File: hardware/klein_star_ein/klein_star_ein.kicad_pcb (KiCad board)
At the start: 6 copper layers, 100 x 90 mm, 138 parts, among them J1 USB_A, J10 AudioJack3_Ground_Switch, J11 AudioJack3_Ground_Switch, J12 AudioJack3_Ground_Switch, J2 DB15_Female_HighDensity_Mount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, J3 Bus_PCI_Express_x1, J4 1367073-1, J5 ARJM11C7-502-AB-ER2-T, J6 USB_C_Receptacle, J7 MEM2051-00-195-00-A, J8 AudioJack3_Ground_Switch, J9 AudioJack3_Ground_Switch, U1 ECP5UM25, U10 SN74ALVC245PWR, U11 KSZ9021RL, U12 TUSB2036, U13 TPS2041B, U2 MT41K512M16, U3 MT41K512M16, U4 FT2232HQ, U5 W25Q128JVS, U6 USB3300-EZK, U7 USB3300-EZK, U8 SN74ALVC245PWR, U9 SN74ALVC245PWR

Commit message: Added decups to KSZ9021
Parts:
- added C67: 22uF, Capacitor_SMD:C_0402_1005Metric, F.Cu at (167.6, 35.6)
- added C68: 22uF, Capacitor_SMD:C_0402_1005Metric, F.Cu at (153.9, 26.6)
- added C69: 22uF, Capacitor_SMD:C_0402_1005Metric, F.Cu at (130.7, 52.7)
- added C70: 22uF, Capacitor_SMD:C_0402_1005Metric, F.Cu at (131.2, 34.5)
- added C71: 22uF, Capacitor_SMD:C_0402_1005Metric, F.Cu at (189.0, 42.7)
- added C72: 22uF, Capacitor_SMD:C_0402_1005Metric, F.Cu at (171.2, 34.7)
- added C73: 22uF, Capacitor_SMD:C_0402_1005Metric, F.Cu at (147.5, 30.9)
- added C74: 22uF, Capacitor_SMD:C_0402_1005Metric, F.Cu at (130.7, 50.7)
- added C75: 22uF, Capacitor_SMD:C_0402_1005Metric, F.Cu at (124.1, 33.9)
- added C76: 22uF, Capacitor_SMD:C_0402_1005Metric, F.Cu at (193.6, 42.6)
- added C77: 0.1uF, Capacitor_SMD:C_0402_1005Metric, F.Cu at (134.9, 114.5)
- added C78: 0.1uF, Capacitor_SMD:C_0402_1005Metric, F.Cu at (140.6, 116.5)
- added C79: 0.1uF, Capacitor_SMD:C_0402_1005Metric, F.Cu at (134.9, 112.5)
- added C80: 0.1uF, Capacitor_SMD:C_0402_1005Metric, F.Cu at (143.5, 112.5)
- added C81: 0.1uF, Capacitor_SMD:C_0402_1005Metric, F.Cu at (137.7, 114.5)
- added C82: 0.1uF, Capacitor_SMD:C_0402_1005Metric, F.Cu at (134.9, 116.5)
- added C83: 0.1uF, Capacitor_SMD:C_0402_1005Metric, F.Cu at (140.6, 114.5)
- added C84: 0.1uF, Capacitor_SMD:C_0402_1005Metric, F.Cu at (137.7, 112.5)
- added C85: 0.1uF, Capacitor_SMD:C_0402_1005Metric, F.Cu at (143.5, 114.5)
- added C86: 0.1uF, Capacitor_SMD:C_0402_1005Metric, F.Cu at (137.7, 116.5)
- added C87: 0.1uF, Capacitor_SMD:C_0402_1005Metric, F.Cu at (143.5, 116.5)
- added C88: 0.1uF, Capacitor_SMD:C_0402_1005Metric, F.Cu at (134.9, 118.5)
- added C89: 0.1uF, Capacitor_SMD:C_0402_1005Metric, F.Cu at (137.7, 118.5)
- added C90: 0.1uF, Capacitor_SMD:C_0402_1005Metric, F.Cu at (132.0, 118.5)
- added C91: 0.1uF, Capacitor_SMD:C_0402_1005Metric, F.Cu at (140.6, 112.5)
- added C92: 0.1uF, Capacitor_SMD:C_0402_1005Metric, F.Cu at (132.0, 114.5)
- added C93: 0.1uF, Capacitor_SMD:C_0402_1005Metric, F.Cu at (132.0, 116.5)
- added C94: 0.1uF, Capacitor_SMD:C_0402_1005Metric, F.Cu at (140.6, 118.5)
- added C95: 0.1uF, Capacitor_SMD:C_0402_1005Metric, F.Cu at (132.0, 112.5)
- added L3: 1uH, Inductor_SMD:L_0603_1608Metric, F.Cu at (170.7, 32.0)
- added L4: 1uH, Inductor_SMD:L_0603_1608Metric, F.Cu at (146.9, 27.3)
- added L5: 1uH, Inductor_SMD:L_0603_1608Metric, F.Cu at (127.8, 47.2)
- added L6: 1uH, Inductor_SMD:L_0603_1608Metric, F.Cu at (131.3, 31.8)
- added L7: 1uH, Inductor_SMD:L_0603_1608Metric, F.Cu at (194.4, 40.7)
- added R1: R220, Resistor_SMD:R_0402_1005Metric_Pad0.72x0.64mm_HandSolder, F.Cu at (116.5, 99.3)
- added R11: 200k, Resistor_SMD:R_0402_1005Metric_Pad0.72x0.64mm_HandSolder, F.Cu at (130.6, 48.6)
- added R12: 200k, Resistor_SMD:R_0402_1005Metric_Pad0.72x0.64mm_HandSolder, F.Cu at (127.5, 49.8)
- added R14: 200k, Resistor_SMD:R_0402_1005Metric_Pad0.72x0.64mm_HandSolder, F.Cu at (124.2, 29.8)
- added R15: 200k, Resistor_SMD:R_0402_1005Metric_Pad0.72x0.64mm_HandSolder, F.Cu at (127.5, 33.8)
- added R16: 200k, Resistor_SMD:R_0402_1005Metric_Pad0.72x0.64mm_HandSolder, F.Cu at (191.4, 40.6)
- added R17: 160k, Resistor_SMD:R_0402_1005Metric_Pad0.72x0.64mm_HandSolder, F.Cu at (194.8, 42.7)
- added R3: R220, Resistor_SMD:R_0402_1005Metric_Pad0.72x0.64mm_HandSolder, F.Cu at (116.2, 114.4)
- added R4: 200k, Resistor_SMD:R_0402_1005Metric_Pad0.72x0.64mm_HandSolder, F.Cu at (174.5, 31.6)
- added R6: 63.2k, Resistor_SMD:R_0402_1005Metric_Pad0.72x0.64mm_HandSolder, F.Cu at (174.1, 34.9)
- added R7: 200k, Resistor_SMD:R_0402_1005Metric_Pad0.72x0.64mm_HandSolder, F.Cu at (154.2, 28.7)
- added R8: 44.2k, Resistor_SMD:R_0402_1005Metric_Pad0.72x0.64mm_HandSolder, F.Cu at (151.5, 29.2)
- added TP3: TestPoint, TestPoint:TestPoint_Pad_1.0x1.0mm, F.Cu at (177.6, 30.9)
- added TP4: TestPoint, TestPoint:TestPoint_Pad_1.0x1.0mm, F.Cu at (150.1, 23.6)
- added TP5: TestPoint, TestPoint:TestPoint_Pad_1.0x1.0mm, F.Cu at (127.6, 52.2)
- added TP6: TestPoint, TestPoint:TestPoint_Pad_1.0x1.0mm, F.Cu at (130.8, 27.5)
- added TP7: TestPoint, TestPoint:TestPoint_Pad_1.0x1.0mm, F.Cu at (188.7, 40.5)
- added U14: AP61300Z6-7, Package_TO_SOT_SMD:SOT-563, F.Cu at (166.2, 32.9)
- added U15: AP61300Z6-7, Package_TO_SOT_SMD:SOT-563, F.Cu at (151.1, 27.4)
- added U16: AP61300Z6-7, Package_TO_SOT_SMD:SOT-563, F.Cu at (131.0, 46.3)
- added U17: AP61300Z6-7, Package_TO_SOT_SMD:SOT-563, F.Cu at (127.7, 30.5)
- added U18: AP61300Z6-7, Package_TO_SOT_SMD:SOT-563, F.Cu at (191.4, 42.8)
- moved C58 61.5 mm to (64.1, 116.8)
- moved U11 1.54 mm to (124.5, 106.5)
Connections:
- J5 pad L1: unconnected-(J5-PadL1) -> Net-(J5-PadL1)
- J5 pad L2: unconnected-(J5-PadL2) -> Net-(J5-PadL2)
- J5 pad L3: unconnected-(J5-PadL3) -> Net-(J5-PadL3)
- J5 pad L4: unconnected-(J5-PadL4) -> Net-(J5-PadL4)
- J5 pad S1: Net-(J5-PadS1) -> GND
- J5 pad S2: Net-(J5-PadS1) -> GND
- J6 pad A1: Net-(J6-PadA1) -> GND
- J6 pad A12: Net-(J6-PadA1) -> GND
- J6 pad A4: Net-(J6-PadA4) -> +5V
- J6 pad A9: Net-(J6-PadA4) -> +5V
- J6 pad B1: Net-(J6-PadA1) -> GND
- J6 pad B12: Net-(J6-PadA1) -> GND
- J6 pad B4: Net-(J6-PadA4) -> +5V
- J6 pad B9: Net-(J6-PadA4) -> +5V
- J6 pad S1: unconnected-(J6-PadS1) -> GND
- U11 pad 12: unconnected-(U11-Pad12) -> +1V2
- U11 pad 13: unconnected-(U11-Pad13) -> +1V2
- U11 pad 16: unconnected-(U11-Pad16) -> +3V3
- U11 pad 19: unconnected-(U11-Pad19) -> Net-(J5-PadL2)
- U11 pad 20: unconnected-(U11-Pad20) -> +3V3
- U11 pad 21: unconnected-(U11-Pad21) -> Net-(J5-PadL4)
- U11 pad 22: unconnected-(U11-Pad22) -> +1V2
- U11 pad 29: unconnected-(U11-Pad29) -> +1V2
- U11 pad 30: unconnected-(U11-Pad30) -> +3V3
- U11 pad 35: unconnected-(U11-Pad35) -> +1V2
- U11 pad 37: unconnected-(U11-Pad37) -> +3V3
- U11 pad 4: unconnected-(U11-Pad4) -> +1V2
- U11 pad 40: unconnected-(U11-Pad40) -> +1V2
- U11 pad 44: unconnected-(U11-Pad44) -> +3V3
- U11 pad 5: unconnected-(U11-Pad5) -> +1V2
- U11 pad 52: unconnected-(U11-Pad52) -> +1V2
- U11 pad 54: unconnected-(U11-Pad54) -> +1V2
- U11 pad 58: unconnected-(U11-Pad58) -> +1V2
- U11 pad 6: unconnected-(U11-Pad6) -> +3V3
- U11 pad 61: unconnected-(U11-Pad61) -> +3V3
- U11 pad 64: unconnected-(U11-Pad64) -> +3V3

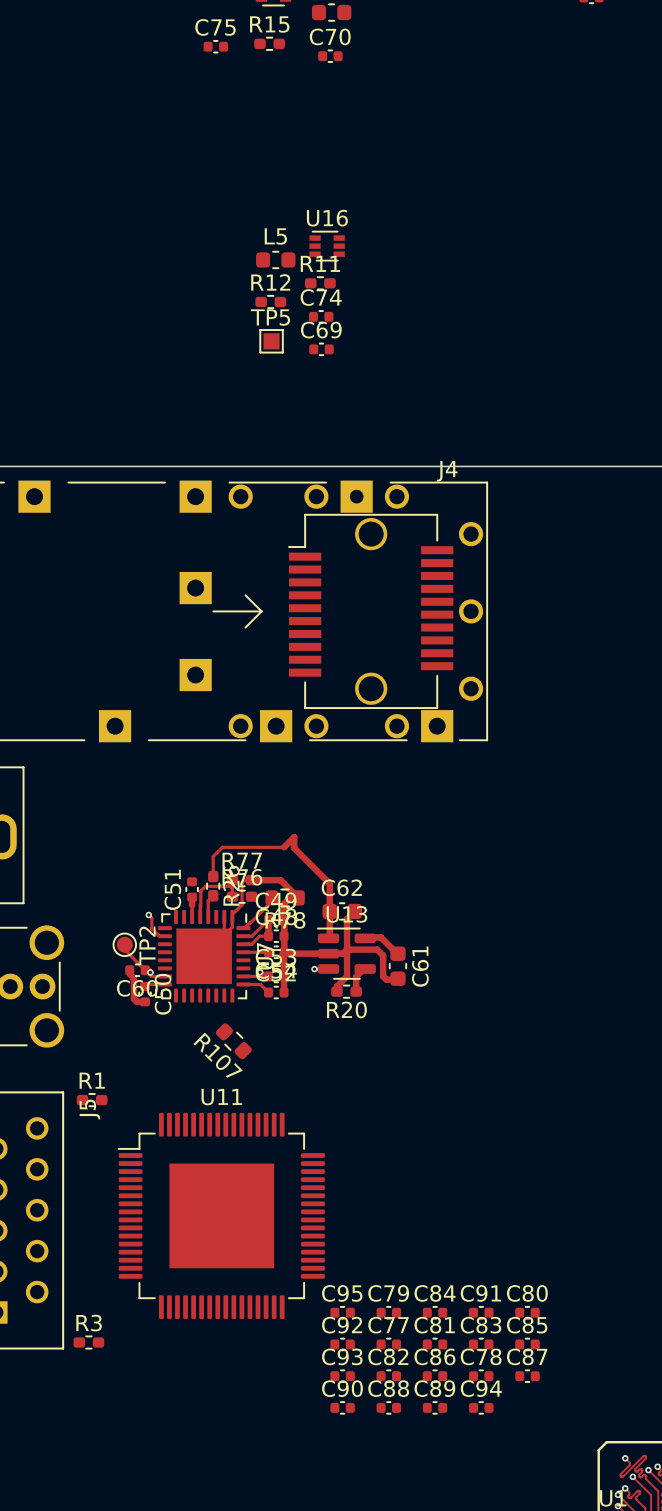
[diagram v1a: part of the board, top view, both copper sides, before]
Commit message: Switched decupling caps to bigger size
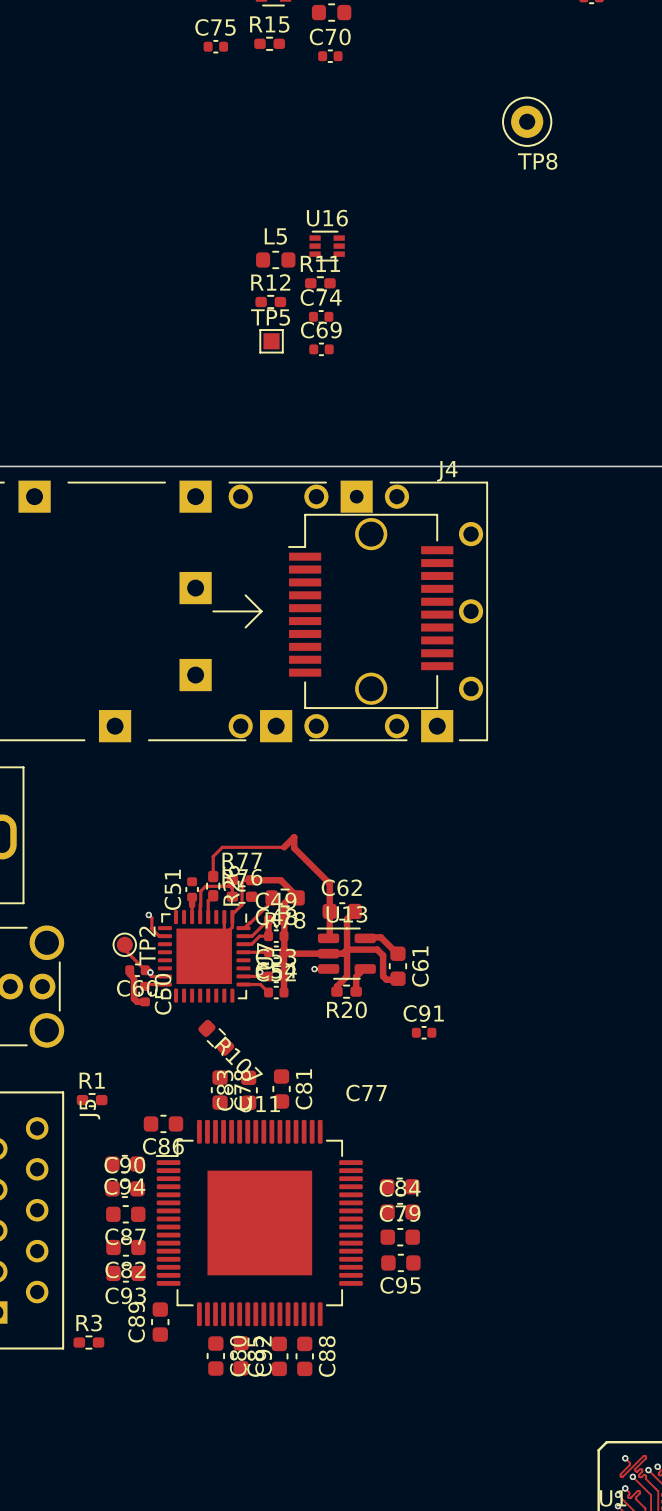
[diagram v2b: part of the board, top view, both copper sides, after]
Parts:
- added TP8: TestPoint, TestPoint:TestPoint_Loop_D1.80mm_Drill1.0mm_Beaded, F.Cu at (143.5, 38.6)
- C77, C78, C79, C80, C81, C82, C83, C84, C85, C86, C87, C88, C89, C90, C92, C93, C94, C95: footprint Capacitor_SMD:C_0402_1005Metric -> Capacitor_SMD:C_0603_1608Metric
- moved C87 26.9 mm to (118.5, 106.4), turned to 180 degrees
- moved C94 26.8 mm to (118.5, 103.3), turned to 180 degrees
- moved C78 24.1 mm to (124.4, 98.7), turned to -90 degrees
- moved C86 23.0 mm to (120.9, 100.8), turned to 180 degrees
- moved C83 21.4 mm to (126.2, 98.7), turned to 90 degrees
- moved C80 19.5 mm to (124.1, 115.2), turned to -90 degrees
- moved C90 19.2 mm to (118.5, 104.8)
- moved C81 18.5 mm to (128.2, 98.7), turned to -90 degrees
- moved C82 18.2 mm to (118.5, 108.5), turned to 180 degrees
- moved C89 17.9 mm to (120.7, 113.1), turned to 90 degrees
- moved C91 17.7 mm to (137.1, 95.2)
- moved C85 15.4 mm to (128.1, 115.2), turned to 90 degrees
- moved C93 14.9 mm to (118.5, 110.1), turned to 180 degrees
- moved C77 9.81 mm to (135.6, 104.7)
- moved C84 6.62 mm to (135.6, 106.3)
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
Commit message: Prototype of power section footprint
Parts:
- C91: footprint Capacitor_SMD:C_0402_1005Metric -> Capacitor_SMD:C_0603_1608Metric
- moved R107 50.5 mm to (74.0, 89.7)
- moved TP8 40.0 mm to (183.4, 40.6)
- moved C76 10.4 mm to (188.5, 33.5), turned to 180 degrees
- moved TP5 10.4 mm to (132.4, 43.0)
- moved R17 9.85 mm to (187.4, 36.3)
- moved U14 9.04 mm to (174.3, 37.0)
- moved C91 8.02 mm to (129.8, 98.7), turned to -90 degrees
- moved TP7 7.64 mm to (190.8, 33.2)
- moved L3 7.49 mm to (176.6, 36.7), turned to -90 degrees
- moved C74 7.25 mm to (129.9, 43.5), turned to 180 degrees
- moved C67 6.92 mm to (173.8, 38.7), turned to 180 degrees
- moved C73 6.82 mm to (150.0, 24.6), turned to 180 degrees
- moved U18 6.79 mm to (189.3, 36.3)
- moved C75 6.75 mm to (126.6, 27.7), turned to 180 degrees
- moved R16 6.75 mm to (188.3, 34.6)
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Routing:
- net 1.35_DRAM: track 0.00 -> 7.55 mm, vias 0 -> 1
- net GND: track 278.7 -> 286.0 mm, vias 79 -> 83
- net +5V: track 2.48 -> 6.72 mm, vias 0 -> 1
- net Net-(R16-Pad2): track 0.00 -> 2.47 mm
- net Net-(L7-Pad1): track 0.00 -> 1.58 mm
